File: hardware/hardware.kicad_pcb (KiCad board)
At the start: 2 copper layers, 38 parts, among them J1 USB_B_Micro, J2 Breakout, Q1 FS8205, U1 DW01+G, U2 TP4056, U3 USBLC6-2, U4 LM317A, U5 PIC18F45K50_QFP

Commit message: Added NLB-310 footprint, symbol & 3D model.
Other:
- copper layers 2 -> 4

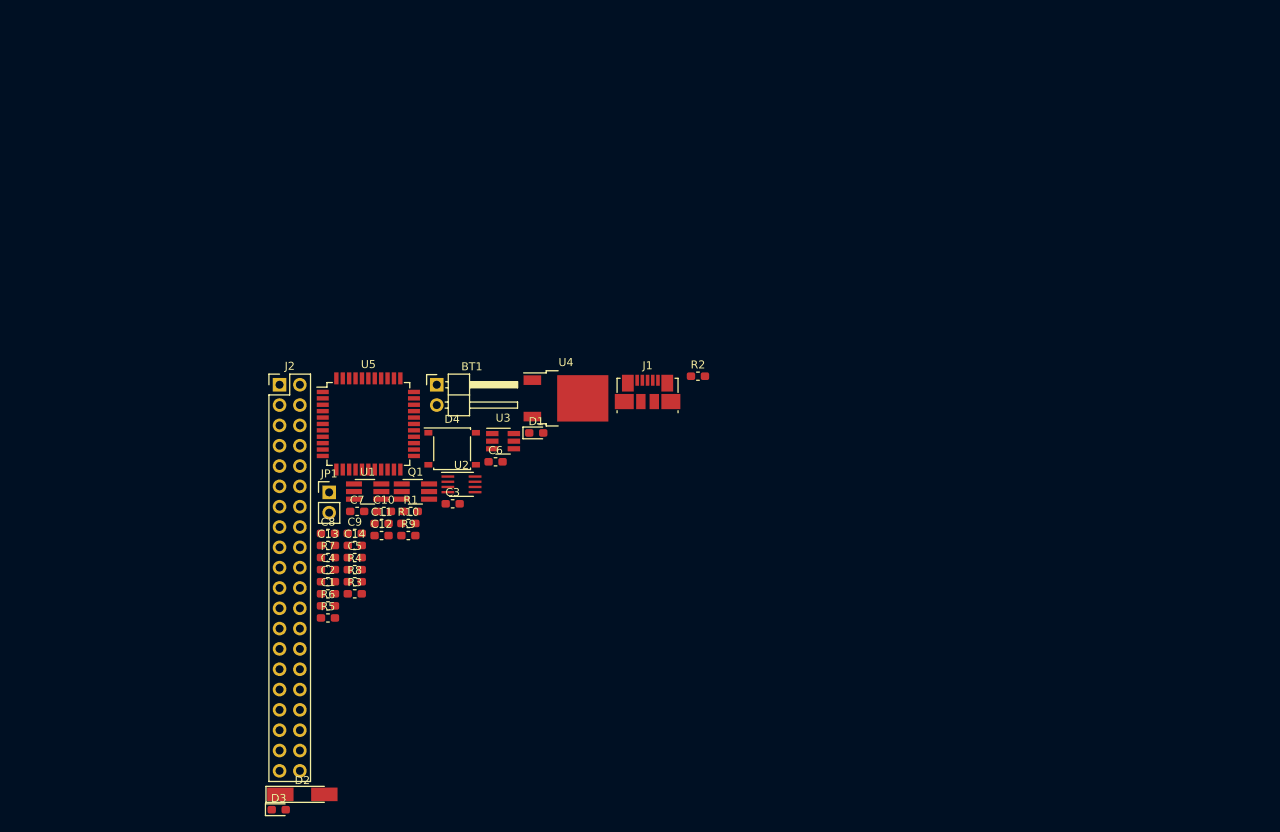
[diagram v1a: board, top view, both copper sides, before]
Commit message: Added TQFN-32 model.
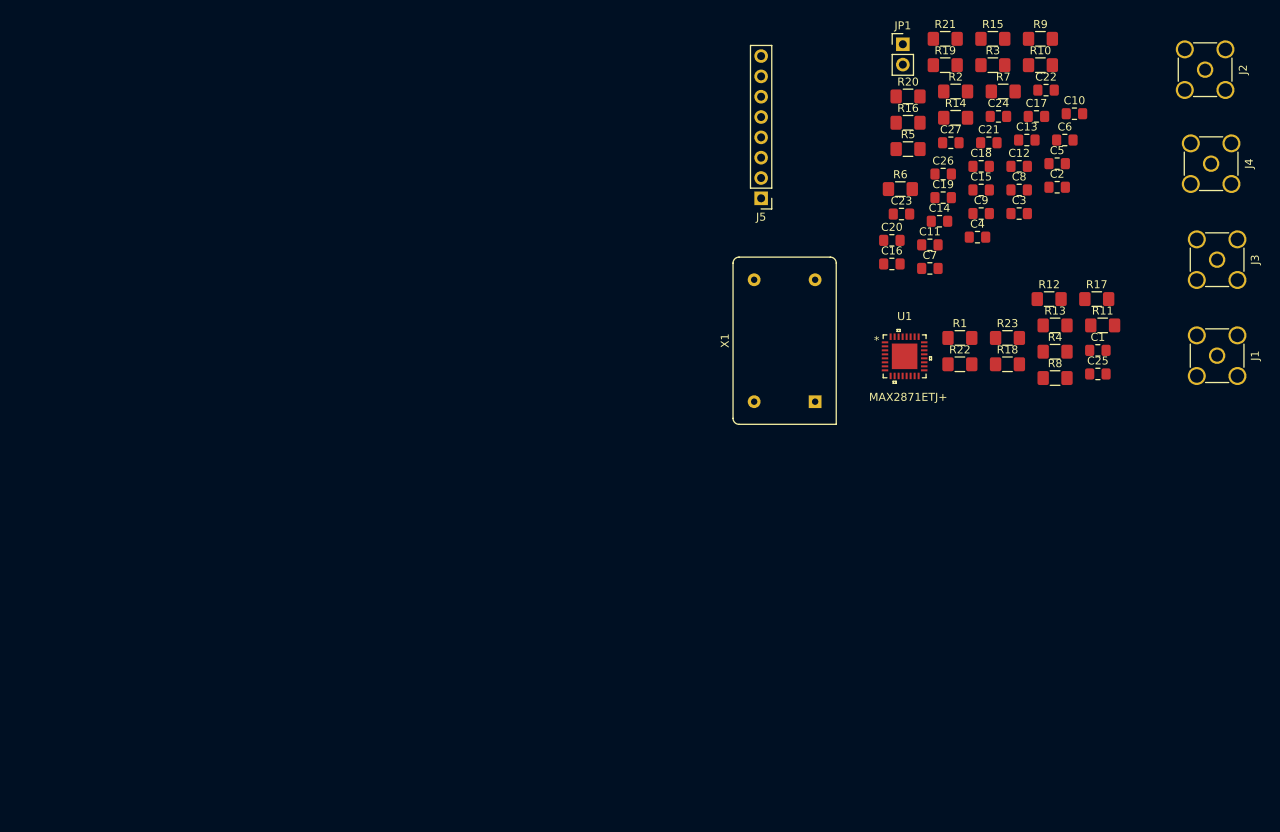
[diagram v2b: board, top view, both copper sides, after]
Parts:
- removed BT1: 3.7V, Connector_PinHeader_2.54mm:PinHeader_1x02_P2.54mm_Horizontal
- removed D1: GHC-YR, LED_SMD:LED_0603_1608Metric_Pad1.05x0.95mm_HandSolder
- removed D2: ZMM5V1, Diode_SMD:D_MiniMELF_Handsoldering
- removed D3: BHC-ZL, LED_SMD:LED_0603_1608Metric_Pad1.05x0.95mm_HandSolder
- removed D4: M7, Diode_SMD:Diode_Bridge_Diotec_ABS
- removed Q1: FS8205, Package_TO_SOT_SMD:TSOT-23-6_HandSoldering
- removed U2: TP4056, Package_SO:SSOP-8_2.95x2.8mm_P0.65mm
- removed U3: USBLC6-2, Package_TO_SOT_SMD:SOT-23-6_Handsoldering
- removed U4: LM317A, Package_TO_SOT_SMD:TO-252-2
- removed U5: PIC18F45K50_QFP, Package_QFP:TQFP-44_10x10mm_P0.8mm
- added C15: 100nF, Capacitor_SMD:C_0805_2012Metric_Pad1.15x1.40mm_HandSolder, F.Cu at (215.3, 44.8)
- added C16: 100p, Capacitor_SMD:C_0805_2012Metric_Pad1.15x1.40mm_HandSolder, F.Cu at (204.1, 54.0)
- added C17: 820pF, Capacitor_SMD:C_0805_2012Metric_Pad1.15x1.40mm_HandSolder, F.Cu at (222.2, 35.6)
- added C18: 12nF, Capacitor_SMD:C_0805_2012Metric_Pad1.15x1.40mm_HandSolder, F.Cu at (215.3, 41.8)
- added C19: 100p, Capacitor_SMD:C_0805_2012Metric_Pad1.15x1.40mm_HandSolder, F.Cu at (210.5, 45.7)
- added C20: 1μF, Capacitor_SMD:C_0805_2012Metric_Pad1.15x1.40mm_HandSolder, F.Cu at (204.1, 51.1)
- added C21: 1μF, Capacitor_SMD:C_0805_2012Metric_Pad1.15x1.40mm_HandSolder, F.Cu at (216.2, 38.9)
- added C22: 1μF, Capacitor_SMD:C_0805_2012Metric_Pad1.15x1.40mm_HandSolder, F.Cu at (223.4, 32.3)
- added C23: 10nF, Capacitor_SMD:C_0805_2012Metric_Pad1.15x1.40mm_HandSolder, F.Cu at (205.3, 47.8)
- added C24: 10nF, Capacitor_SMD:C_0805_2012Metric_Pad1.15x1.40mm_HandSolder, F.Cu at (217.4, 35.6)
- added C25: 0.1μF, Capacitor_SMD:C_0805_2012Metric_Pad1.15x1.40mm_HandSolder, F.Cu at (229.8, 67.8)
- added C26: 0.1μF, Capacitor_SMD:C_0805_2012Metric_Pad1.15x1.40mm_HandSolder, F.Cu at (210.5, 42.8)
- added C27: 10nF, Capacitor_SMD:C_0805_2012Metric_Pad1.15x1.40mm_HandSolder, F.Cu at (211.5, 38.9)
- added J3: RF B-N, Connector_Coaxial:SMA_Amphenol_901-144_Vertical, F.Cu at (244.8, 53.5)
- added J4: RF B-P, Connector_Coaxial:SMA_Amphenol_901-144_Vertical, F.Cu at (244.0, 41.5)
- added J5: Breakout, Connector_PinHeader_2.54mm:PinHeader_1x08_P2.54mm_Vertical, F.Cu at (187.8, 45.8)
- added R11: 18, Resistor_SMD:R_1206_3216Metric_Pad1.42x1.75mm_HandSolder, F.Cu at (230.4, 61.7)
- added R12: 300, Resistor_SMD:R_1206_3216Metric_Pad1.42x1.75mm_HandSolder, F.Cu at (223.8, 58.4)
- added R13: 300, Resistor_SMD:R_1206_3216Metric_Pad1.42x1.75mm_HandSolder, F.Cu at (224.5, 61.7)
- added R14: 18, Resistor_SMD:R_1206_3216Metric_Pad1.42x1.75mm_HandSolder, F.Cu at (212.1, 35.8)
- added R15: 300, Resistor_SMD:R_1206_3216Metric_Pad1.42x1.75mm_HandSolder, F.Cu at (216.7, 25.9)
- added R16: 300, Resistor_SMD:R_1206_3216Metric_Pad1.42x1.75mm_HandSolder, F.Cu at (206.1, 36.4)
- added R17: 0, Resistor_SMD:R_1206_3216Metric_Pad1.42x1.75mm_HandSolder, F.Cu at (229.7, 58.4)
- added R18: 120, Resistor_SMD:R_1206_3216Metric_Pad1.42x1.75mm_HandSolder, F.Cu at (218.5, 66.6)
- added R19: 0, Resistor_SMD:R_1206_3216Metric_Pad1.42x1.75mm_HandSolder, F.Cu at (210.8, 29.2)
- added R20: 120, Resistor_SMD:R_1206_3216Metric_Pad1.42x1.75mm_HandSolder, F.Cu at (206.1, 33.1)
- added R21: 0, Resistor_SMD:R_1206_3216Metric_Pad1.42x1.75mm_HandSolder, F.Cu at (210.8, 25.9)
- added R22: 120, Resistor_SMD:R_1206_3216Metric_Pad1.42x1.75mm_HandSolder, F.Cu at (212.6, 66.6)
- added R23: 1m, Resistor_SMD:R_1206_3216Metric_Pad1.42x1.75mm_HandSolder, F.Cu at (218.5, 63.3)
- added X1: CXO_DIP14, Oscillator:Oscillator_DIP-14, F.Cu at (194.5, 71.2)
- C1, C11: value 10μF -> 100pf; footprint Capacitor_SMD:C_0603_1608Metric_Pad1.05x0.95mm_HandSolder -> Capacitor_SMD:C_0805_2012Metric_Pad1.15x1.40mm_HandSolder
- C10, C4, C8: value 0.1μF -> 10nF; footprint Capacitor_SMD:C_0603_1608Metric_Pad1.05x0.95mm_HandSolder -> Capacitor_SMD:C_0805_2012Metric_Pad1.15x1.40mm_HandSolder
- C12, C2, C6: value 10μF -> 10nF; footprint Capacitor_SMD:C_0603_1608Metric_Pad1.05x0.95mm_HandSolder -> Capacitor_SMD:C_0805_2012Metric_Pad1.15x1.40mm_HandSolder
- C13: value 1μF -> 100p; footprint Capacitor_SMD:C_0603_1608Metric_Pad1.05x0.95mm_HandSolder -> Capacitor_SMD:C_0805_2012Metric_Pad1.15x1.40mm_HandSolder
- C14: value 0.1μF -> 100p; footprint Capacitor_SMD:C_0603_1608Metric_Pad1.05x0.95mm_HandSolder -> Capacitor_SMD:C_0805_2012Metric_Pad1.15x1.40mm_HandSolder
- C3: value 100nF -> 100pf; footprint Capacitor_SMD:C_0603_1608Metric_Pad1.05x0.95mm_HandSolder -> Capacitor_SMD:C_0805_2012Metric_Pad1.15x1.40mm_HandSolder
- C5, C7, C9: value 0.1μF -> 100pf; footprint Capacitor_SMD:C_0603_1608Metric_Pad1.05x0.95mm_HandSolder -> Capacitor_SMD:C_0805_2012Metric_Pad1.15x1.40mm_HandSolder
- J1: value USB_B_Micro -> RF A-N; footprint Connector_USB:USB_Micro-B_Molex_47346-0001 -> Connector_Coaxial:SMA_Amphenol_901-144_Vertical
- J2: value Breakout -> RF A-P; footprint Connector_PinHeader_2.54mm:PinHeader_2x20_P2.54mm_Vertical -> Connector_Coaxial:SMA_Amphenol_901-144_Vertical
- JP1: value Jumper -> SW
- R1: value 180 -> 18; footprint Resistor_SMD:R_0603_1608Metric_Pad1.05x0.95mm_HandSolder -> Resistor_SMD:R_1206_3216Metric_Pad1.42x1.75mm_HandSolder
- R10: value 480 -> 90; footprint Resistor_SMD:R_0603_1608Metric_Pad1.05x0.95mm_HandSolder -> Resistor_SMD:R_1206_3216Metric_Pad1.42x1.75mm_HandSolder
- R2, R3: value 68 -> 300; footprint Resistor_SMD:R_0603_1608Metric_Pad1.05x0.95mm_HandSolder -> Resistor_SMD:R_1206_3216Metric_Pad1.42x1.75mm_HandSolder
- R4: value 100 -> 18; footprint Resistor_SMD:R_0603_1608Metric_Pad1.05x0.95mm_HandSolder -> Resistor_SMD:R_1206_3216Metric_Pad1.42x1.75mm_HandSolder
- R5: value 2k -> 300; footprint Resistor_SMD:R_0603_1608Metric_Pad1.05x0.95mm_HandSolder -> Resistor_SMD:R_1206_3216Metric_Pad1.42x1.75mm_HandSolder
- R6: value 1k -> 300; footprint Resistor_SMD:R_0603_1608Metric_Pad1.05x0.95mm_HandSolder -> Resistor_SMD:R_1206_3216Metric_Pad1.42x1.75mm_HandSolder
- R7: value 1k -> 4.7k; footprint Resistor_SMD:R_0603_1608Metric_Pad1.05x0.95mm_HandSolder -> Resistor_SMD:R_1206_3216Metric_Pad1.42x1.75mm_HandSolder
- R8: value 1.5k -> 240; footprint Resistor_SMD:R_0603_1608Metric_Pad1.05x0.95mm_HandSolder -> Resistor_SMD:R_1206_3216Metric_Pad1.42x1.75mm_HandSolder
- R9: value 10k -> 30; footprint Resistor_SMD:R_0603_1608Metric_Pad1.05x0.95mm_HandSolder -> Resistor_SMD:R_1206_3216Metric_Pad1.42x1.75mm_HandSolder
- U1: value DW01+G -> MAX2871ETJ+; footprint Package_TO_SOT_SMD:TSOT-23-6_HandSoldering -> MAX:MAX2871ETJ+
- moved J2 122.2 mm to (243.2, 29.8), turned to 270 degrees
- moved C2 103.6 mm to (224.8, 44.4)
- moved R3 103.6 mm to (216.7, 29.2)
- moved R7 102.6 mm to (218.0, 32.5)
- moved C13 101.0 mm to (221.0, 38.5)
- moved C1 100.9 mm to (229.8, 64.8)
- moved C5 100.7 mm to (224.8, 41.5)
- moved R9 100.5 mm to (222.7, 25.9)
- moved C10 99.6 mm to (226.9, 35.3)
- moved R10 97.6 mm to (222.7, 29.2)
- moved C8 96.5 mm to (220.0, 44.8)
- moved R5 93.2 mm to (206.1, 39.7)
- moved C12 92.1 mm to (220.0, 41.8)
- moved R4 91.7 mm to (224.5, 65.0)
- moved C4 91.2 mm to (214.8, 50.7)
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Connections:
- C1 pad 1: Net-(C1-Pad1) -> GND
- C1 pad 2: BAT- -> VCC_CP
- C10 pad 1: VDD -> VCC_CP
- C10 pad 2: BAT- -> GND
- C11 pad 1: VDD -> VCC_CP
- C11 pad 2: BAT- -> GND
- C12 pad 1: Net-(C12-Pad1) -> VCC_CP
- C12 pad 2: BAT- -> GND
- C13 pad 1: VDD -> RF_A_N
- C13 pad 2: BAT- -> Net-(C13-Pad2)
- C14 pad 1: Net-(C14-Pad1) -> RF_A_P
- C14 pad 2: BAT- -> Net-(C14-Pad2)
- C2 pad 1: BP_VDD -> GND
- C2 pad 2: BAT- -> VCC_CP
- C3 pad 1: BAT- -> GND
- C3 pad 2: USB_VBUS -> VCC_CP
- C4 pad 1: BP_VDD -> GND
- C4 pad 2: BAT- -> VCC_CP
- C5 pad 1: BP_VDD -> GND
- C5 pad 2: BAT- -> VCC_CP
- C6 pad 1: VDD -> GND
- C6 pad 2: BAT- -> VCC_CP
- C7 pad 1: VDD -> VCC_CP
- C7 pad 2: BAT- -> GND
- C8 pad 1: VDD -> VCC_CP
- C8 pad 2: BAT- -> GND
- C9 pad 1: VDD -> VCC_CP
- C9 pad 2: BAT- -> GND
- J1 pad 1: USB_VBUS -> Net-(J1-Pad1)
- J2 pad 1: VDD -> Net-(J2-Pad1)
- J2 pad 2: BAT- -> Net-(J2-Pad2)
- JP1 pad 2: Net-(C14-Pad1) -> SW
- R1 pad 1: Net-(C1-Pad1) -> Net-(J1-Pad1)
- R1 pad 2: USB_VBUS -> Net-(C13-Pad2)
- R10 pad 1: Net-(JP1-Pad1) -> GND
- R10 pad 2: IC_MCLR -> Net-(JP1-Pad1)
- R2 pad 1: Net-(R2-Pad1) -> Net-(C13-Pad2)
- R2 pad 2: Net-(D3-Pad1) -> Net-(J1-Pad2)
- R3 pad 1: Net-(R3-Pad1) -> Net-(J1-Pad1)
- R3 pad 2: Net-(D1-Pad1) -> Net-(J1-Pad2)
- R4 pad 1: BP_VDD -> Net-(J2-Pad1)
- R4 pad 2: BAT+ -> Net-(C14-Pad2)
- R5 pad 1: Net-(R5-Pad1) -> Net-(C14-Pad2)
- R5 pad 2: BAT- -> Net-(J2-Pad2)
- R6 pad 1: BP_CS -> Net-(J2-Pad1)
- R6 pad 2: Net-(Q1-Pad3) -> Net-(J2-Pad2)
- R7 pad 1: VDD -> Net-(R7-Pad1)
- R7 pad 2: Net-(C12-Pad1) -> GND
- R8 pad 1: Net-(C12-Pad1) -> CP_OUT
- R8 pad 2: BAT- -> TUNE
- R9 pad 1: VDD -> Net-(JP1-Pad1)
- R9 pad 2: Net-(JP1-Pad1) -> Net-(C15-Pad1)
- U1 pad 1: BP_OD -> CLK
- U1 pad 2: BP_CS -> DATA
- U1 pad 3: BP_OC -> LE
- U1 pad 4: Net-(U1-Pad4) -> CE
- U1 pad 5: BP_VDD -> SW
- U1 pad 6: BAT- -> VCC_CP

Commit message: Fixed minor issue with RF Output.
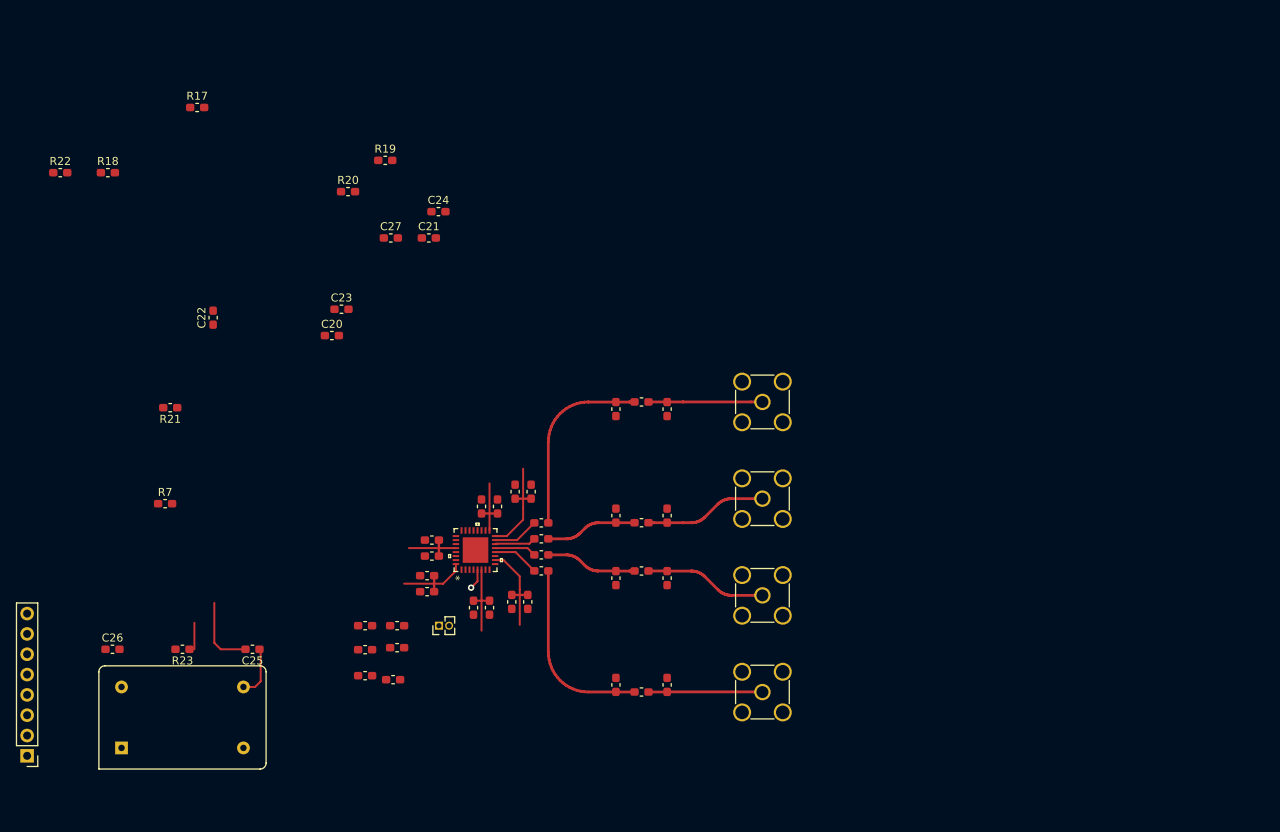
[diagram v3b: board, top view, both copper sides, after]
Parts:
- C1, C10, C11, C12, C13, C14, C15, C16, C17, C18, C19, C2, C20, C21, C22, C23, C24, C25, C26, C27, C3, C4, C5, C6, C7, C8, C9: footprint Capacitor_SMD:C_0805_2012Metric_Pad1.15x1.40mm_HandSolder -> Capacitor_SMD:C_0603_1608Metric_Pad1.05x0.95mm_HandSolder
- JP1: footprint Connector_PinHeader_2.54mm:PinHeader_1x02_P2.54mm_Vertical -> Connector_PinHeader_1.27mm:PinHeader_1x02_P1.27mm_Vertical
- R1, R10, R11, R12, R13, R14, R15, R16, R17, R18, R19, R2, R20, R21, R22, R23, R3, R4, R5, R6, R7, R8, R9: footprint Resistor_SMD:R_1206_3216Metric_Pad1.42x1.75mm_HandSolder -> Resistor_SMD:R_0603_1608Metric_Pad1.05x0.95mm_HandSolder
- moved C26 119.6 mm to (106.7, 102.2)
- moved R7 116.7 mm to (113.2, 84.0)
- moved R9 116.0 mm to (138.2, 105.5)
- moved J5 115.2 mm to (96.0, 115.5)
- moved R17 115.0 mm to (117.3, 34.5)
- moved R18 115.0 mm to (106.1, 42.6)
- moved R22 115.0 mm to (100.1, 42.6)
- moved R10 111.6 mm to (141.8, 106.0)
- moved C25 111.1 mm to (124.2, 102.2), turned to 180 degrees
- moved R23 110.2 mm to (115.4, 102.2), turned to 180 degrees
- moved C22 107.9 mm to (119.2, 60.8), turned to 90 degrees
- moved R21 107.3 mm to (113.9, 72.0), turned to 180 degrees
- moved C17 102.2 mm to (142.2, 99.2), turned to 180 degrees
- moved C10 99.4 mm to (146.0, 93.0), turned to 180 degrees
- moved X1 96.9 mm to (107.8, 114.5), turned to 0 degrees
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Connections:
- net Net-(U1-Pad25) renamed LD
- J1 pad 2: Net-(J1-Pad2) -> GND
- J2 pad 2: Net-(J2-Pad2) -> GND
- J3 pad 2: Net-(J3-Pad2) -> GND
- J4 pad 2: Net-(J4-Pad2) -> GND
- R12 pad 2: Net-(J3-Pad2) -> GND
- R13 pad 2: Net-(J3-Pad2) -> GND
- R15 pad 2: Net-(J4-Pad2) -> GND
- R16 pad 2: Net-(J4-Pad2) -> GND
- R2 pad 2: Net-(J1-Pad2) -> GND
- R3 pad 2: Net-(J1-Pad2) -> GND
- R5 pad 2: Net-(J2-Pad2) -> GND
- R6 pad 2: Net-(J2-Pad2) -> GND
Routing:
- net VCC_CP: track 0.00 -> 60.1 mm
- net Net-(C14-Pad2): track 0.00 -> 23.8 mm
- net Net-(C16-Pad2): track 0.00 -> 23.8 mm
- net Net-(J4-Pad1): track 0.00 -> 15.4 mm
- net Net-(J1-Pad1): track 0.00 -> 15.3 mm
- net Net-(J2-Pad1): track 0.00 -> 14.3 mm
- net Net-(J3-Pad1): track 0.00 -> 14.2 mm
- net RF_REF: track 0.00 -> 12.4 mm
- net Net-(C13-Pad2): track 0.00 -> 11.5 mm
- net Net-(C19-Pad2): track 0.00 -> 11.4 mm
- net Net-(C25-Pad1): track 0.00 -> 6.45 mm
- net RF_A_P: track 0.00 -> 5.87 mm
- net RF_B_N: track 0.00 -> 5.79 mm
- net RF_A_N: track 0.00 -> 5.25 mm
- net RF_B_P: track 0.00 -> 5.17 mm
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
